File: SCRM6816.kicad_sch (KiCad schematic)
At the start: 10 parts, among them U1 68HC000P16, U2 74HC04, U24 74HC08, U6 74HC32, U7 74HC14, U8 74HC05, X1 CXO_DIP8_16MHz

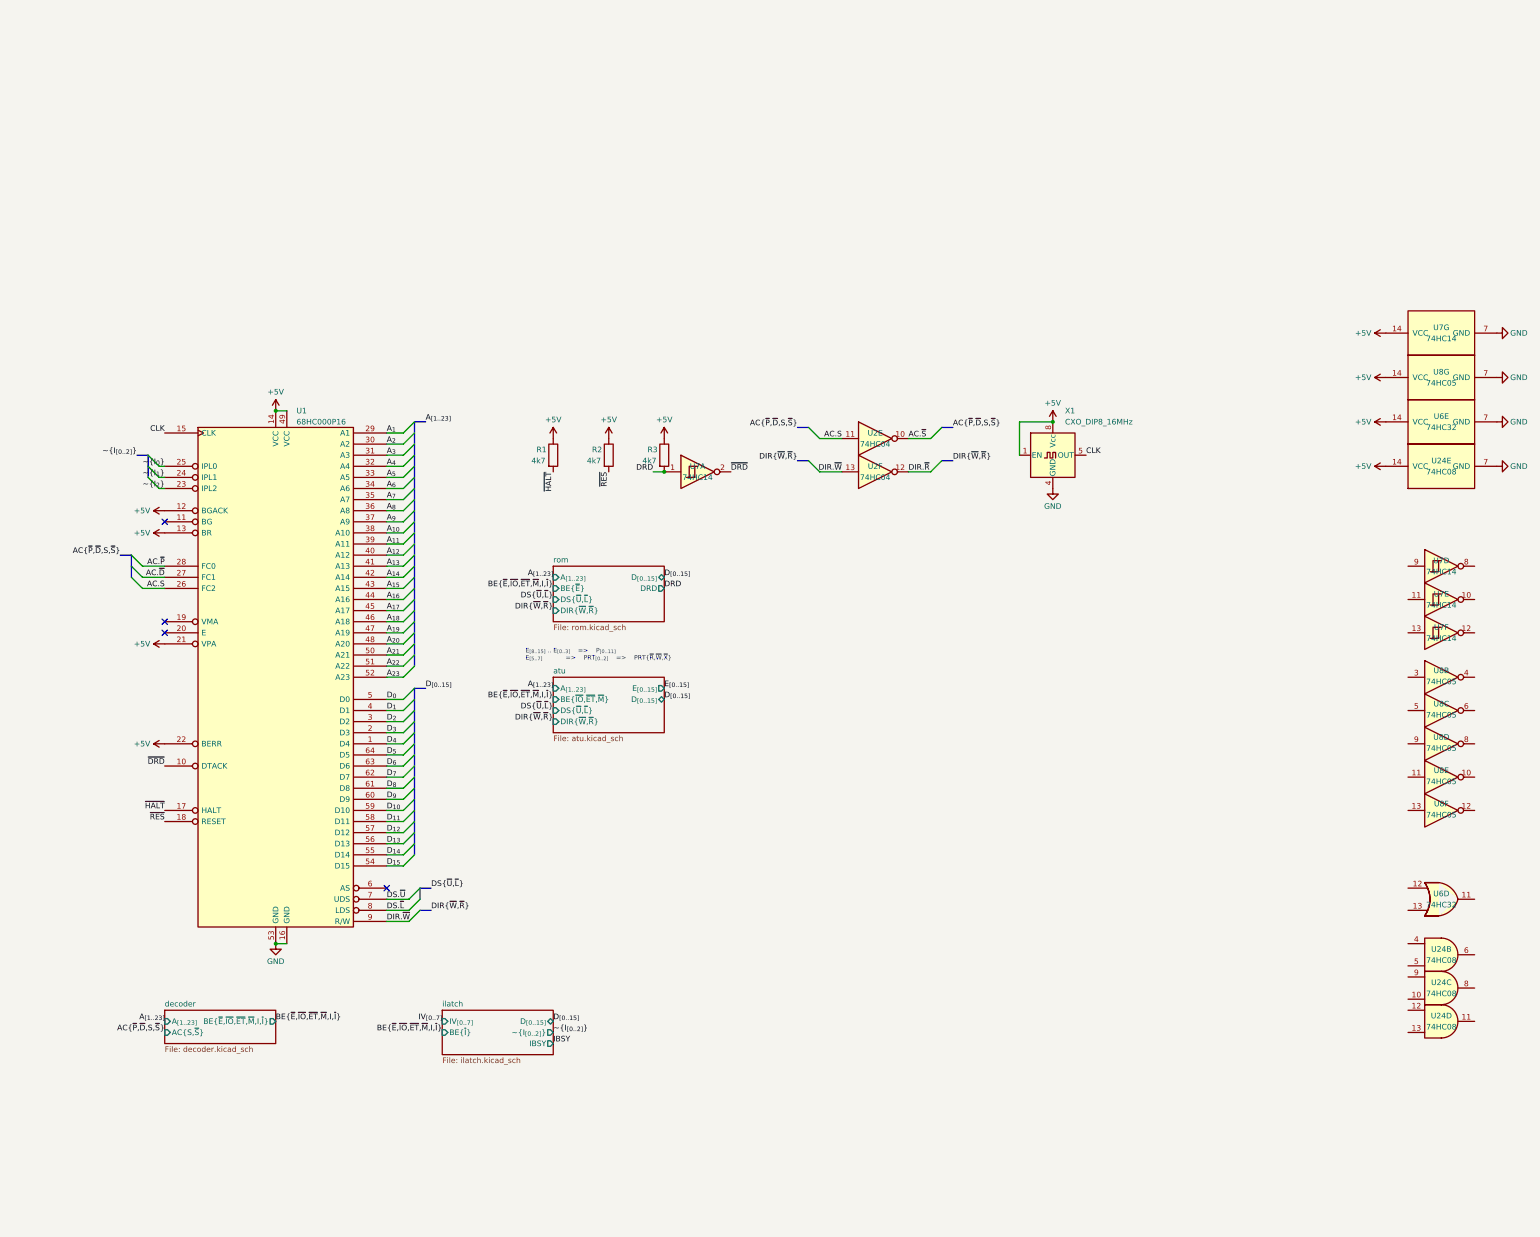
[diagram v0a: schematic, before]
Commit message: finished scheme, footprints not completely assigned yet
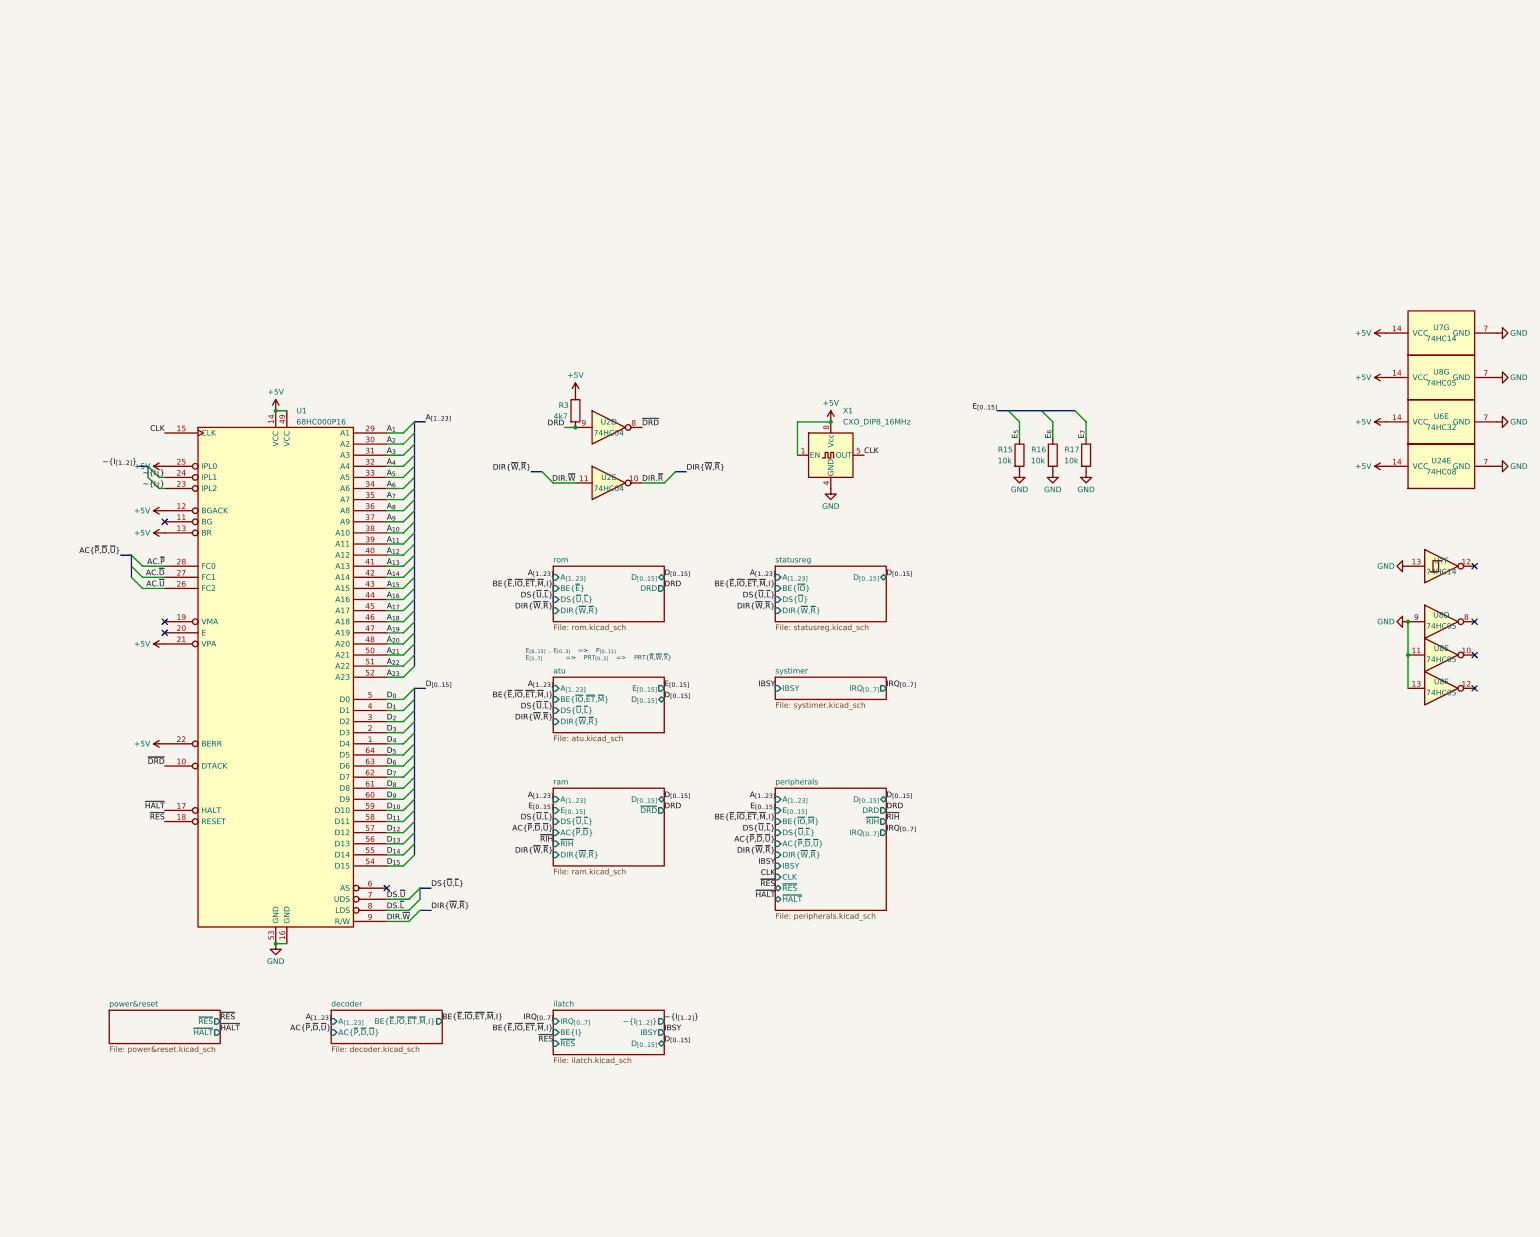
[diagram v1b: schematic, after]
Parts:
- removed R1, R2: 4k7, Resistor_THT:R_Axial_DIN0207_L6.3mm_D2.5mm_P2.54mm_Vertical, symbol Device:R
- removed unit 6 of U2
- removed unit 2 of U24
- removed unit 4 of U24
- removed unit 3 of U24
- removed unit 4 of U6
- removed unit 1 of U7
- removed unit 4 of U7
- removed unit 5 of U7
- removed unit 2 of U8
- removed unit 3 of U8
- added R15, R16, R17: 10k, Resistor_THT:R_Axial_DIN0207_L6.3mm_D2.5mm_P2.54mm_Vertical, symbol Device:R
- added unit 4 of U2
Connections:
- net AC.~{S} is gone; now on net DIR.~{R}: U2.10
- net ~{I_{0}} is gone; now on net +5V: U1.25 (IPL0)
- net DIR.~{W}: now also U2.11
- net DRD: now also U2.9
- net GND: now also U7.13, U8.11, U8.13, U8.9, R15.2, R16.2, R17.2
- net ~{DRD}: now also U2.8
- net AC.S renamed AC.~{U}
- net AC.~{U}: no longer U2.11
- new net E_{5}: R15.1
- new net E_{6}: R16.1
- new net E_{7}: R17.1
- no-connect marks 4 -> 8
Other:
- added sheet peripherals (peripherals.kicad_sch)
- added sheet power&reset (power&reset.kicad_sch)
- added sheet ram (ram.kicad_sch)
- added sheet statusreg (statusreg.kicad_sch)
- added sheet systimer (systimer.kicad_sch)
- sheet decoder ports: added AC{~{P},~{D},~{U}}, BE{~{E},~{IO},~{ET},~{M},I}; removed AC{S,~{S}}, BE{~{E},~{IO},~{ET},~{M},I,~{I}}
- sheet ilatch ports: added BE{I}, IRQ_{[0..7]}, ~{I_{[1..2]}}, ~{RES}; removed BE{~{I}}, IV_{[0..7]}, ~{I_{[0..2]}}
- moved on the sheet: R3, U2E, U8E, U8F, X1

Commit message: done the pcb layout + added the 1M ram bank project
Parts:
- U1: footprint Package_DIP:DIP-64_W22.86mm_Socket -> Package_DIP:DIP-64_W22.86mm
- U2, U24, U6, U7, U8: footprint Package_DIP:DIP-14_W7.62mm_Socket -> Package_DIP:DIP-14_W7.62mm
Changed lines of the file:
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@@
 			)
 		)
-		(property "Footprint" "Package_DIP:DIP-14_W7.62mm_Socket"
+		(property "Footprint" "Package_DIP:DIP-14_W7.62mm"
 			(at 139.7 31.75 0)
 			(effects
@@
 			)
 		)
-		(property "Footprint" "Package_DIP:DIP-14_W7.62mm_Socket"
+		(property "Footprint" "Package_DIP:DIP-14_W7.62mm"
 			(at 139.7 44.45 0)
 			(effects
@@
 			)
 		)
-		(property "Footprint" "Package_DIP:DIP-14_W7.62mm_Socket"
+		(property "Footprint" "Package_DIP:DIP-14_W7.62mm"
 			(at 330.2 63.5 0)
 			(effects
@@
 			)
 		)
-		(property "Footprint" "Package_DIP:DIP-14_W7.62mm_Socket"
+		(property "Footprint" "Package_DIP:DIP-14_W7.62mm"
 			(at 330.2 83.82 0)
 			(effects
@@
 			)
 		)
-		(property "Footprint" "Package_DIP:DIP-14_W7.62mm_Socket"
+		(property "Footprint" "Package_DIP:DIP-14_W7.62mm"
 			(at 330.2 40.64 0)
 			(effects
@@
 			)
 		)
-		(property "Footprint" "Package_DIP:DIP-14_W7.62mm_Socket"
+		(property "Footprint" "Package_DIP:DIP-14_W7.62mm"
 			(at 330.2 91.44 0)
 			(effects
@@
 			)
 		)
-		(property "Footprint" "Package_DIP:DIP-64_W22.86mm_Socket"
+		(property "Footprint" "Package_DIP:DIP-64_W22.86mm"
 			(at 63.5 88.9 0)
 			(effects
@@
 			)
 		)
-		(property "Footprint" "Package_DIP:DIP-14_W7.62mm_Socket"
+		(property "Footprint" "Package_DIP:DIP-14_W7.62mm"
 			(at 330.2 76.2 0)
 			(effects
@@
 			)
 		)
-		(property "Footprint" "Package_DIP:DIP-14_W7.62mm_Socket"
+		(property "Footprint" "Package_DIP:DIP-14_W7.62mm"
 			(at 330.2 10.16 0)
 			(effects
@@
 			)
 		)
-		(property "Footprint" "Package_DIP:DIP-14_W7.62mm_Socket"
+		(property "Footprint" "Package_DIP:DIP-14_W7.62mm"
 			(at 330.2 30.48 0)
 			(effects
@@
 			)
 		)
-		(property "Footprint" "Package_DIP:DIP-14_W7.62mm_Socket"
+		(property "Footprint" "Package_DIP:DIP-14_W7.62mm"
 			(at 330.2 20.32 0)
 			(effects

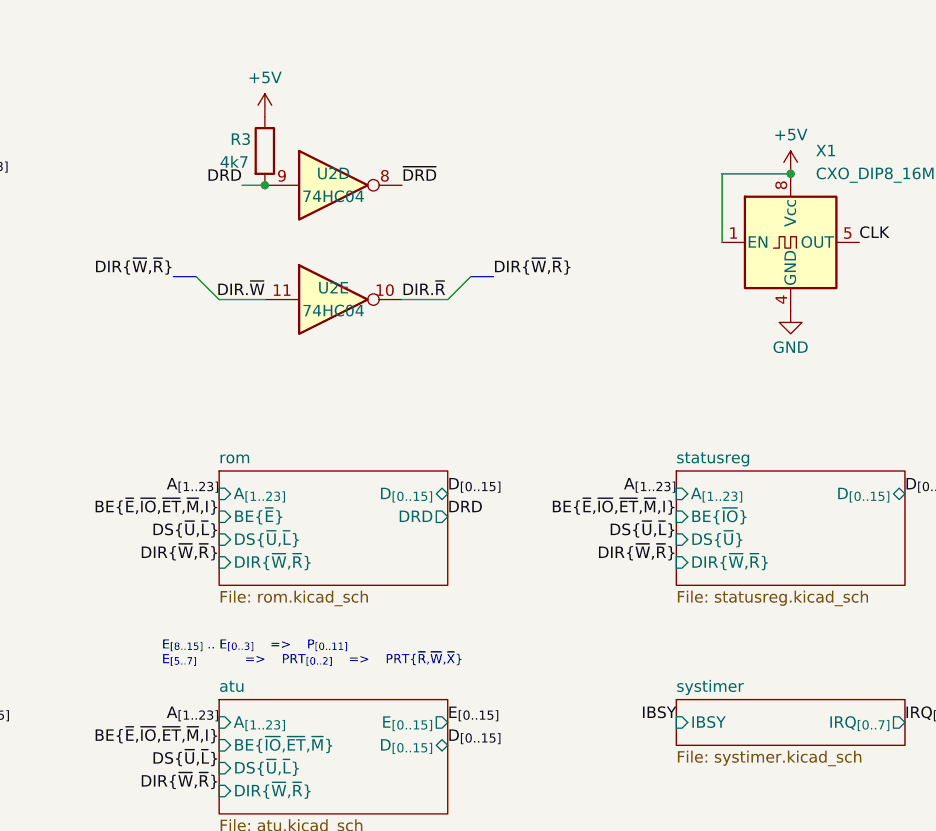
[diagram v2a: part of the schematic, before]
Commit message: updated scheme: 	- fixed E to P & PRT mapping 	- swapped root's 04 couple with the 14's of pidreg & statusreg
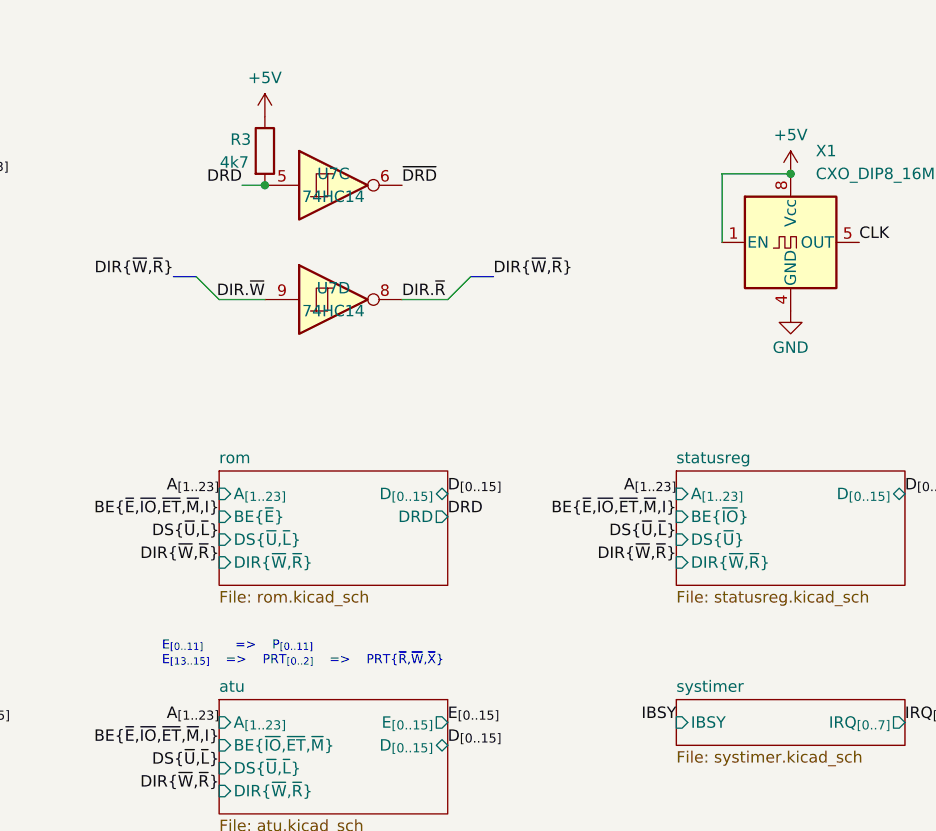
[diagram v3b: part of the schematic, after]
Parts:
- removed U2: 74HC04, Package_DIP:DIP-14_W7.62mm, symbol 74xx:74LS04
- added unit 3 of U7
- added unit 4 of U7
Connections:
- net DIR.~{R}: now also U7.8
- net DIR.~{W}: now also U7.9
- net DRD: now also U7.5
- net ~{DRD}: now also U7.6
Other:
- note added: "E_{[0..11]} => P_{[0..11]} E_{[13..15]} => PRT_{[0..2]} => PRT{~{R},~{W},~{X}}"
- note removed: "E_{[8..15]} .. E_{[0..3]} => P_{[0..11]} E_{[5..7]} => PRT_{[0..2]} => PRT{~{R},~{W},~{X}}"
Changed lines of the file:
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@@
 	(generator_version "9.0")
 	(paper "A4")
-	(text "E_{[8..15]} .. E_{[0..3]}	=>	P_{[0..11]}\nE_{[5..7]}			=>	PRT_{[0..2]}	=>	PRT{~{R},~{W},~{X}}"
+	(text "E_{[0..11]}		=>	P_{[0..11]}\nE_{[13..15]}	=>	PRT_{[0..2]}	=>	PRT{~{R},~{W},~{X}}"
 		(exclude_from_sim no)
 		(at 120.65 83.82 0)
@@
 	)
 	(symbol
-		(lib_id "74xx:74LS04")
-		(at 139.7 31.75 0)
-		(unit 4)
-		(exclude_from_sim no)
-		(in_bom yes)
-		(on_board yes)
-		(dnp no)
-		(property "Reference" "U2"
-			(at 139.7 30.48 0)
-			(effects
-				(font
-					(size 1.27 1.27)
-				)
-			)
-		)
-		(property "Value" "74HC04"
-			(at 139.7 33.02 0)
-			(effects
-				(font
-					(size 1.27 1.27)
-				)
-			)
-		)
-		(property "Footprint" "Package_DIP:DIP-14_W7.62mm"
-			(at 139.7 31.75 0)
-			(effects
-				(font
-					(size 1.27 1.27)
-				)
-				(hide yes)
-			)
-		)
-		(property "Datasheet" "http://www.ti.com/lit/gpn/sn74LS04"
-			(at 139.7 31.75 0)
-			(effects
-				(font
-					(size 1.27 1.27)
-				)
-				(hide yes)
-			)
-		)
-		(property "Description" "Hex Inverter"
-			(at 139.7 31.75 0)
-			(effects
-				(font
-					(size 1.27 1.27)
-				)
-				(hide yes)
-			)
-		)
-		(pin "11"
-		)
-		(pin "7"
-		)
-		(pin "5"
-		)
-		(pin "4"
-		)
-		(pin "3"
-		)
-		(pin "2"
-		)
-		(pin "9"
-		)
-		(pin "14"
-		)
-		(pin "6"
-		)
-		(pin "1"
-		)
-		(pin "8"
-		)
-		(pin "10"
-		)
-		(pin "12"
-		)
-		(pin "13"
-		)
-		(instances
-			(project "SCRM6816"
-				(path "/56448118-82b3-4e1c-bda3-84d63e01a14a"
-					(reference "U2")
-					(unit 4)
-				)
-			)
-		)
-	)
-	(symbol
-		(lib_id "74xx:74LS04")
-		(at 139.7 44.45 0)
-		(unit 5)
-		(exclude_from_sim no)
-		(in_bom yes)
-		(on_board yes)
-		(dnp no)
-		(property "Reference" "U2"
-			(at 139.7 43.18 0)
-			(effects
-				(font
-					(size 1.27 1.27)
-				)
-			)
-		)
-		(property "Value" "74HC04"
-			(at 139.7 45.72 0)
-			(effects
-				(font
-					(size 1.27 1.27)
-				)
-			)
-		)
-		(property "Footprint" "Package_DIP:DIP-14_W7.62mm"
-			(at 139.7 44.45 0)
-			(effects
-				(font
-					(size 1.27 1.27)
-				)
-				(hide yes)
-			)
-		)
-		(property "Datasheet" "http://www.ti.com/lit/gpn/sn74LS04"
-			(at 139.7 44.45 0)
-			(effects
-				(font
-					(size 1.27 1.27)
-				)
-				(hide yes)
-			)
-		)
-		(property "Description" "Hex Inverter"
-			(at 139.7 44.45 0)
-			(effects
-				(font
-					(size 1.27 1.27)
-				)
-				(hide yes)
-			)
-		)
-		(pin "11"
-		)
-		(pin "7"
-		)
-		(pin "5"
-		)
-		(pin "4"
-		)
-		(pin "3"
-		)
-		(pin "2"
-		)
-		(pin "9"
-		)
-		(pin "14"
-		)
-		(pin "6"
-		)
-		(pin "1"
-		)
-		(pin "8"
-		)
-		(pin "10"
-		)
-		(pin "12"
-		)
-		(pin "13"
-		)
-		(instances
-			(project "SCRM6816"
-				(path "/56448118-82b3-4e1c-bda3-84d63e01a14a"
-					(reference "U2")
-					(unit 5)
-				)
-			)
-		)
-	)
-	(symbol
 		(lib_id "power:GND")
 		(at 342.9 30.48 90)
@@
 	)
 	(symbol
+		(lib_id "74xx:74HC14")
+		(at 139.7 31.75 0)
+		(unit 3)
+		(exclude_from_sim no)
+		(in_bom yes)
+		(on_board yes)
+		(dnp no)
+		(property "Reference" "U7"
+			(at 139.7 30.48 0)
+			(effects
+				(font
+					(size 1.27 1.27)
+				)
+			)
+		)
+		(property "Value" "74HC14"
+			(at 139.7 33.02 0)
+			(effects
+				(font
+					(size 1.27 1.27)
+				)
+			)
+		)
+		(property "Footprint" "Package_DIP:DIP-14_W7.62mm"
+			(at 139.7 31.75 0)
+			(effects
+				(font
+					(size 1.27 1.27)
+				)
+				(hide yes)
+			)
+		)
+		(property "Datasheet" "http://www.ti.com/lit/gpn/sn74HC14"
+			(at 139.7 31.75 0)
+			(effects
+				(font
+					(size 1.27 1.27)
+				)
+				(hide yes)
+			)
+		)
+		(property "Description" "Hex inverter schmitt trigger"
+			(at 139.7 31.75 0)
+			(effects
+				(font
+					(size 1.27 1.27)
+				)
+				(hide yes)
+			)
+		)
+		(pin "1"
+		)
+		(pin "5"
+		)
+		(pin "6"
+		)
+		(pin "4"
+		)
+		(pin "2"
+		)
+		(pin "8"
+		)
+		(pin "9"
+		)
+		(pin "3"
+		)
+		(pin "12"
+		)
+		(pin "10"
+		)
+		(pin "7"
+		)
+		(pin "13"
+		)
+		(pin "14"
+		)
+		(pin "11"
+		)
+		(instances
+			(project "SCRM6816"
+				(path "/56448118-82b3-4e1c-bda3-84d63e01a14a"
+					(reference "U7")
+					(unit 3)
+				)
+			)
+		)
+	)
+	(symbol
 		(lib_id "power:GND")
 		(at 233.68 41.91 0)
@@
 				)
 			)
+		)
+	)
+	(symbol
+		(lib_id "74xx:74HC14")
+		(at 139.7 44.45 0)
+		(unit 4)
+		(exclude_from_sim no)
+		(in_bom yes)
+		(on_board yes)
+		(dnp no)
+		(property "Reference" "U7"
+			(at 139.7 43.18 0)
+			(effects
+				(font
+					(size 1.27 1.27)
+				)
+			)
+		)
+		(property "Value" "74HC14"
+			(at 139.7 45.72 0)
+			(effects
+				(font
+					(size 1.27 1.27)
+				)
+			)
+		)
+		(property "Footprint" "Package_DIP:DIP-14_W7.62mm"
+			(at 139.7 44.45 0)
+			(effects
+				(font
+					(size 1.27 1.27)
+				)
+				(hide yes)
+			)
+		)
+		(property "Datasheet" "http://www.ti.com/lit/gpn/sn74HC14"
+			(at 139.7 44.45 0)
+			(effects
+				(font
+					(size 1.27 1.27)
+				)
+				(hide yes)
+			)
+		)
+		(property "Description" "Hex inverter schmitt trigger"
+			(at 139.7 44.45 0)
+			(effects
+				(font
+					(size 1.27 1.27)
+				)
+				(hide yes)
+			)
+		)
+		(pin "1"
+		)
+		(pin "5"
+		)
+		(pin "6"
+		)
+		(pin "4"
+		)
+		(pin "2"
+		)
+		(pin "8"
+		)
+		(pin "9"
+		)
+		(pin "3"
+		)
+		(pin "12"
+		)
+		(pin "10"
+		)
+		(pin "7"
+		)
+		(pin "13"
+		)
+		(pin "14"
+		)
+		(pin "11"
+		)
+		(instances
+			(project "SCRM6816"
+				(path "/56448118-82b3-4e1c-bda3-84d63e01a14a"
+					(reference "U7")
+					(unit 4)
+				)
+			)
